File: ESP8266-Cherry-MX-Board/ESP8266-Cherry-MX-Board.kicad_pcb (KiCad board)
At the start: 2 copper layers, 33 x 90 mm, 63 parts, among them J1 Conn_01x04_Male, J2 USB_C_Receptacle_USB2.0, J3 Conn_01x02, J4 Conn_01x07_Male, SW1 SW_SPST, SW2 SW_SPST, SW3 SW_SPST, SW4 SW_SPST, SW5 PEC11L-4115F-S0020, SW7 SW_Push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

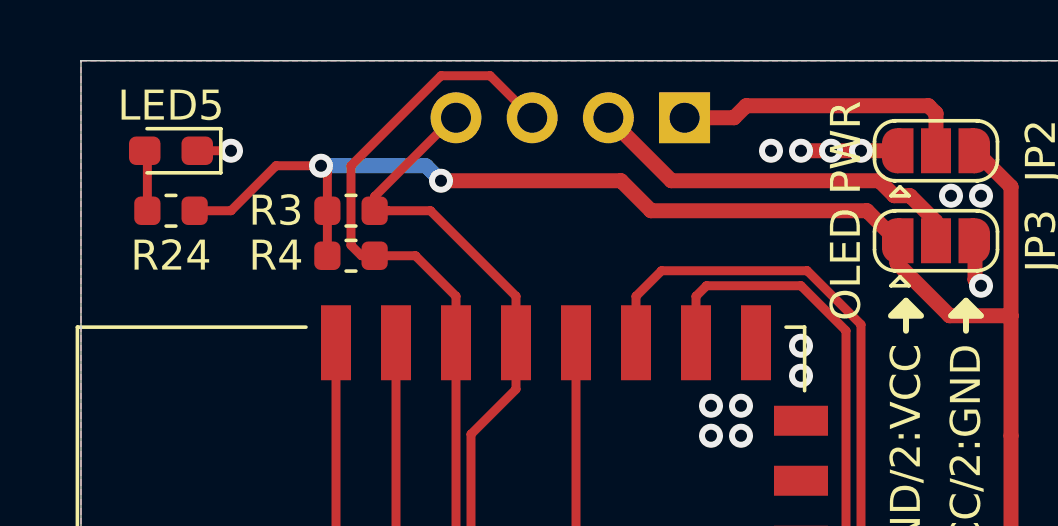
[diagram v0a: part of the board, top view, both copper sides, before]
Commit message: Cleanup of schematic and silkscreen.
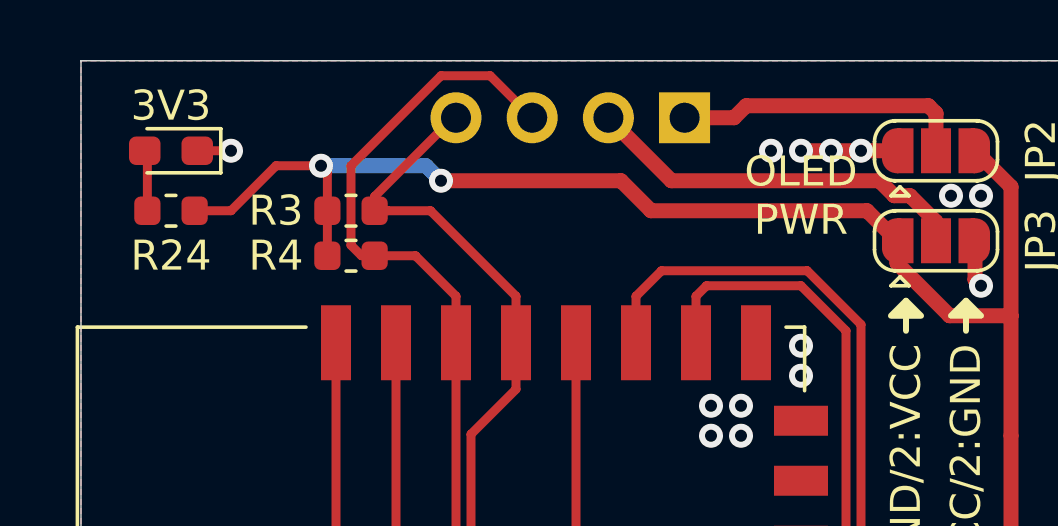
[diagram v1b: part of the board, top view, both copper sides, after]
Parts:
- renumbered LED5 to 3V3
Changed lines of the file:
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@@
   (net 38 /GPIO16)
   (net 39 "Net-(C2-Pad1)")
-  (net 40 "Net-(LED5-Pad2)")
-  (net 41 /GPIO0)
-  (net 42 "Net-(R18-Pad2)")
-  (net 43 "Net-(JP5-Pad2)")
+  (net 40 /GPIO0)
+  (net 41 "Net-(R18-Pad2)")
+  (net 42 "Net-(JP5-Pad2)")
+  (net 43 "Net-(3V3-Pad2)")
   (net_class Default "This is the default net class."
     (clearance 0.2)
@@
     (add_net /~RST~)
     (add_net GND)
+    (add_net "Net-(3V3-Pad2)")
     (add_net "Net-(C2-Pad1)")
     (add_net "Net-(C3-Pad1)")
     (add_net "Net-(J2-PadA5)")
+    (add_net "Net-(J2-PadA6)")
+    (add_net "Net-(J2-PadA7)")
+    (add_net "Net-(J2-PadA8)")
     (add_net "Net-(J2-PadB5)")
+    (add_net "Net-(J2-PadB6)")
+    (add_net "Net-(J2-PadB7)")
+    (add_net "Net-(J2-PadB8)")
     (add_net "Net-(JP1-Pad2)")
     (add_net "Net-(JP2-Pad2)")
@@
     (add_net "Net-(LED3-Pad1)")
     (add_net "Net-(LED4-Pad1)")
-    (add_net "Net-(LED5-Pad2)")
     (add_net "Net-(R15-Pad2)")
     (add_net "Net-(R18-Pad2)")
@@
     (add_net "Net-(R21-Pad2)")
     (add_net "Net-(R23-Pad2)")
+    (add_net "Net-(U1-Pad10)")
+    (add_net "Net-(U1-Pad11)")
+    (add_net "Net-(U1-Pad12)")
+    (add_net "Net-(U1-Pad13)")
+    (add_net "Net-(U1-Pad14)")
+    (add_net "Net-(U1-Pad9)")
+    (add_net "Net-(U2-Pad1)")
+    (add_net "Net-(U5-Pad5)")
     (add_net VBUS)
   )
@@
     (fp_line (start -1.2 1.2) (end -0.9 1.5) (layer F.SilkS) (width 0.12))
     (pad 2 smd rect (at 0 0 180) (size 1 1.5) (layers F.Cu F.Mask)
-      (net 43 "Net-(JP5-Pad2)"))
+      (net 42 "Net-(JP5-Pad2)"))
     (pad 3 smd custom (at 1.3 0 180) (size 1 0.5) (layers F.Cu F.Mask)
       (net 39 "Net-(C2-Pad1)") (zone_connect 2)
@@
     (fp_line (start -0.8 0.4) (end -0.8 -0.4) (layer F.Fab) (width 0.1))
     (pad 2 smd roundrect (at 0.7875 0 180) (size 0.875 0.95) (layers F.Cu F.Paste F.Mask) (roundrect_rratio 0.25)
-      (net 40 "Net-(LED5-Pad2)"))
+      (net 43 "Net-(3V3-Pad2)"))
     (pad 1 smd roundrect (at -0.7875 0 180) (size 0.875 0.95) (layers F.Cu F.Paste F.Mask) (roundrect_rratio 0.25)
       (net 4 +3V3))
@@
     (tags "LED handsolder")
     (attr smd)
-    (fp_text reference LED5 (at 0 1.5) (layer F.SilkS)
+    (fp_text reference 3V3 (at 0 1.5) (layer F.SilkS)
       (effects (font (size 1 1) (thickness 0.15)))
     )
@@
     (fp_line (start 0.8 -0.4) (end -0.5 -0.4) (layer F.Fab) (width 0.1))
     (pad 2 smd roundrect (at 0.875 0 180) (size 1.05 0.95) (layers F.Cu F.Paste F.Mask) (roundrect_rratio 0.25)
-      (net 40 "Net-(LED5-Pad2)"))
+      (net 43 "Net-(3V3-Pad2)"))
     (pad 1 smd roundrect (at -0.875 0 180) (size 1.05 0.95) (layers F.Cu F.Paste F.Mask) (roundrect_rratio 0.25)
       (net 3 GND))
@@
     (fp_line (start -2.7 1.7) (end -2.7 -1.7) (layer B.CrtYd) (width 0.05))
     (pad 1 smd rect (at -2.275 0 180) (size 0.65 1.6) (layers B.Cu B.Paste B.Mask)
-      (net 41 /GPIO0))
+      (net 40 /GPIO0))
     (pad 2 smd rect (at 2.275 0 180) (size 0.65 1.6) (layers B.Cu B.Paste B.Mask)
       (net 3 GND))
@@
     (fp_line (start -0.8 0.4) (end -0.8 -0.4) (layer F.Fab) (width 0.1))
     (pad 2 smd roundrect (at 0.7875 0 270) (size 0.875 0.95) (layers F.Cu F.Paste F.Mask) (roundrect_rratio 0.25)
-      (net 42 "Net-(R18-Pad2)"))
+      (net 41 "Net-(R18-Pad2)"))
     (pad 1 smd roundrect (at -0.7875 0 270) (size 0.875 0.95) (layers F.Cu F.Paste F.Mask) (roundrect_rratio 0.25)
       (net 30 /ENCODER_B))
@@
       (net 3 GND))
     (pad B thru_hole circle (at 0 -5 180) (size 2 2) (drill 1) (layers *.Cu *.Mask)
-      (net 42 "Net-(R18-Pad2)"))
+      (net 41 "Net-(R18-Pad2)"))
     (pad MP thru_hole circle (at 7.5 3.1 180) (size 3.2 3.2) (drill 2.6) (layers *.Cu *.Mask))
     (pad MP thru_hole circle (at 7.5 -8.1 180) (size 3.2 3.2) (drill 2.6) (layers *.Cu *.Mask))
@@
       (net 4 +3V3))
     (pad 1 smd roundrect (at -0.7875 0 180) (size 0.875 0.95) (layers F.Cu F.Paste F.Mask) (roundrect_rratio 0.25)
-      (net 41 /GPIO0))
+      (net 40 /GPIO0))
     (model ${KISYS3DMOD}/Resistor_SMD.3dshapes/R_0603_1608Metric.wrl
       (at (xyz 0 0 0))
@@
       (net 3 GND) (solder_mask_margin 0.07) (solder_paste_margin -0.025))
     (pad 8 smd oval (at 1.475 0) (size 0.85 0.28) (layers F.Cu F.Paste F.Mask)
-      (net 43 "Net-(JP5-Pad2)") (solder_mask_margin 0.07) (solder_paste_margin -0.025))
+      (net 42 "Net-(JP5-Pad2)") (solder_mask_margin 0.07) (solder_paste_margin -0.025))
     (pad 7 smd rect (at 1.76 0.5) (size 0.28 0.28) (layers F.Cu F.Paste F.Mask)
       (net 16 "Net-(R19-Pad2)") (solder_mask_margin 0.07) (solder_paste_margin -0.025))
@@
       (net 3 GND) (solder_mask_margin 0.07) (solder_paste_margin -0.025))
     (pad 8 smd rect (at 1.76 0) (size 0.28 0.28) (layers F.Cu F.Paste F.Mask)
-      (net 43 "Net-(JP5-Pad2)") (solder_mask_margin 0.07) (solder_paste_margin -0.025))
+      (net 42 "Net-(JP5-Pad2)") (solder_mask_margin 0.07) (solder_paste_margin -0.025))
     (pad 7 smd oval (at 1.475 0.5) (size 0.85 0.28) (layers F.Cu F.Paste F.Mask)
       (net 16 "Net-(R19-Pad2)") (solder_mask_margin 0.07) (solder_paste_margin -0.025))
@@
       (net 5 /I2C_SDA))
     (pad 18 smd rect (at 7.6 4.5 90) (size 2.5 1) (layers F.Cu F.Paste F.Mask)
-      (net 41 /GPIO0))
+      (net 40 /GPIO0))
     (pad 17 smd rect (at 7.6 6.5 90) (size 2.5 1) (layers F.Cu F.Paste F.Mask)
       (net 34 /GPIO2))
@@
   (gr_poly (pts (xy 162 38.5) (xy 161 38.5) (xy 161.5 38)) (layer F.SilkS) (width 0.2))
   (gr_line (start 161.5 39) (end 161.5 38) (layer F.SilkS) (width 0.2))
-  (gr_text "OLED PWR" (at 159.5 35 90) (layer F.SilkS)
+  (gr_text "OLED\nPWR" (at 158 34.5) (layer F.SilkS)
     (effects (font (size 1 1) (thickness 0.15)))
   )
@@
   (segment (start 153.5 103) (end 153.5 102) (width 0.3) (layer F.Cu) (net 39))
   (segment (start 154.7 104.2) (end 153.5 103) (width 0.3) (layer F.Cu) (net 39))
-  (segment (start 136.2125 33.0875) (end 136.125 33) (width 0.3) (layer F.Cu) (net 40))
-  (segment (start 136.2125 35) (end 136.2125 33.0875) (width 0.3) (layer F.Cu) (net 40))
-  (segment (start 138.2875 60.525) (end 138.5 60.3125) (width 0.3) (layer F.Cu) (net 41))
-  (segment (start 138.2875 61) (end 138.2875 60.525) (width 0.3) (layer F.Cu) (net 41))
-  (via (at 138.5 60) (size 0.8) (drill 0.4) (layers F.Cu B.Cu) (net 41))
-  (segment (start 138.5 60.3125) (end 138.5 60) (width 0.3) (layer F.Cu) (net 41))
-  (segment (start 138.775 60) (end 139.775 61) (width 0.3) (layer B.Cu) (net 41))
-  (segment (start 138.5 60) (end 138.775 60) (width 0.3) (layer B.Cu) (net 41))
-  (segment (start 140.5 61) (end 138.2875 61) (width 0.3) (layer F.Cu) (net 41))
-  (segment (start 141.5 60) (end 140.5 61) (width 0.3) (layer F.Cu) (net 41))
-  (segment (start 150.5 39.4) (end 150.5 50) (width 0.3) (layer F.Cu) (net 41))
-  (segment (start 142 51.5) (end 141.5 52) (width 0.3) (layer F.Cu) (net 41))
-  (segment (start 150.5 50) (end 149 51.5) (width 0.3) (layer F.Cu) (net 41))
-  (segment (start 141.5 52) (end 141.5 60) (width 0.3) (layer F.Cu) (net 41))
-  (segment (start 149 51.5) (end 142 51.5) (width 0.3) (layer F.Cu) (net 41))
-  (segment (start 156.7875 71) (end 156 71.7875) (width 0.3) (layer F.Cu) (net 42))
-  (segment (start 158 71) (end 156.7875 71) (width 0.3) (layer F.Cu) (net 42))
-  (segment (start 155.75 99.25) (end 156 99.5) (width 0.3) (layer F.Cu) (net 43))
-  (segment (start 151.975 100) (end 153.75815 100) (width 0.3) (layer F.Cu) (net 43))
-  (segment (start 153.75815 100) (end 154.50815 99.25) (width 0.3) (layer F.Cu) (net 43))
-  (segment (start 156 99.5) (end 156 103.45) (width 0.3) (layer F.Cu) (net 43))
-  (segment (start 154.50815 99.25) (end 155.75 99.25) (width 0.3) (layer F.Cu) (net 43))
-  (segment (start 156 103.45) (end 156 105) (width 0.3) (layer F.Cu) (net 43))
+  (segment (start 136.2125 33.0875) (end 136.125 33) (width 0.3) (layer F.Cu) (net 43))
+  (segment (start 136.2125 35) (end 136.2125 33.0875) (width 0.3) (layer F.Cu) (net 43))
+  (segment (start 138.2875 60.525) (end 138.5 60.3125) (width 0.3) (layer F.Cu) (net 40))
+  (segment (start 138.2875 61) (end 138.2875 60.525) (width 0.3) (layer F.Cu) (net 40))
+  (via (at 138.5 60) (size 0.8) (drill 0.4) (layers F.Cu B.Cu) (net 40))
+  (segment (start 138.5 60.3125) (end 138.5 60) (width 0.3) (layer F.Cu) (net 40))
+  (segment (start 138.775 60) (end 139.775 61) (width 0.3) (layer B.Cu) (net 40))
+  (segment (start 138.5 60) (end 138.775 60) (width 0.3) (layer B.Cu) (net 40))
+  (segment (start 140.5 61) (end 138.2875 61) (width 0.3) (layer F.Cu) (net 40))
+  (segment (start 141.5 60) (end 140.5 61) (width 0.3) (layer F.Cu) (net 40))
+  (segment (start 150.5 39.4) (end 150.5 50) (width 0.3) (layer F.Cu) (net 40))
+  (segment (start 142 51.5) (end 141.5 52) (width 0.3) (layer F.Cu) (net 40))
+  (segment (start 150.5 50) (end 149 51.5) (width 0.3) (layer F.Cu) (net 40))
+  (segment (start 141.5 52) (end 141.5 60) (width 0.3) (layer F.Cu) (net 40))
+  (segment (start 149 51.5) (end 142 51.5) (width 0.3) (layer F.Cu) (net 40))
+  (segment (start 156.7875 71) (end 156 71.7875) (width 0.3) (layer F.Cu) (net 41))
+  (segment (start 158 71) (end 156.7875 71) (width 0.3) (layer F.Cu) (net 41))
+  (segment (start 155.75 99.25) (end 156 99.5) (width 0.3) (layer F.Cu) (net 42))
+  (segment (start 151.975 100) (end 153.75815 100) (width 0.3) (layer F.Cu) (net 42))
+  (segment (start 153.75815 100) (end 154.50815 99.25) (width 0.3) (layer F.Cu) (net 42))
+  (segment (start 156 99.5) (end 156 103.45) (width 0.3) (layer F.Cu) (net 42))
+  (segment (start 154.50815 99.25) (end 155.75 99.25) (width 0.3) (layer F.Cu) (net 42))
+  (segment (start 156 103.45) (end 156 105) (width 0.3) (layer F.Cu) (net 42))
   (zone (net 0) (net_name "") (layers F&B.Cu) (hatch edge 0.508)
     (connect_pads (clearance 0.508))
